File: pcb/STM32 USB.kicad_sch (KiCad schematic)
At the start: 8 parts, among them U1 STM32L432KBUx

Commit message: Pushbutton for reset
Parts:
- added C8: 0.1uF, Capacitor_SMD:C_0201_0603Metric, symbol Device:C
- added SW1: 222AMVBAR, SO4_222A-M-V-B_CTS, symbol 222AMVBAR:222AMVBAR
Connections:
- net GND: now also C8.2, SW1.4
- net NRST: now also C8.1, SW1.3

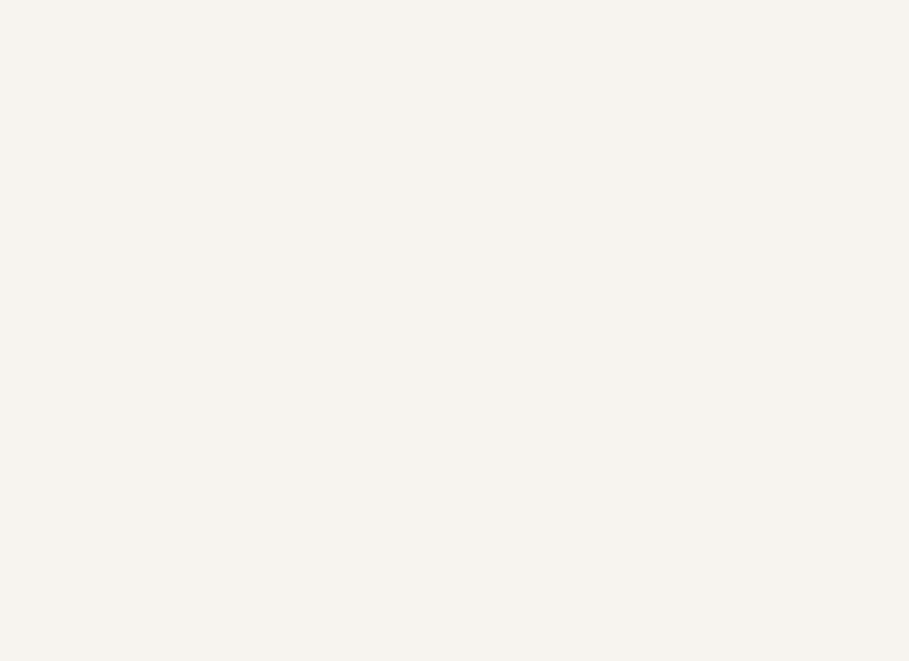
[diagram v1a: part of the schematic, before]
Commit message: Added USB C components to schematic
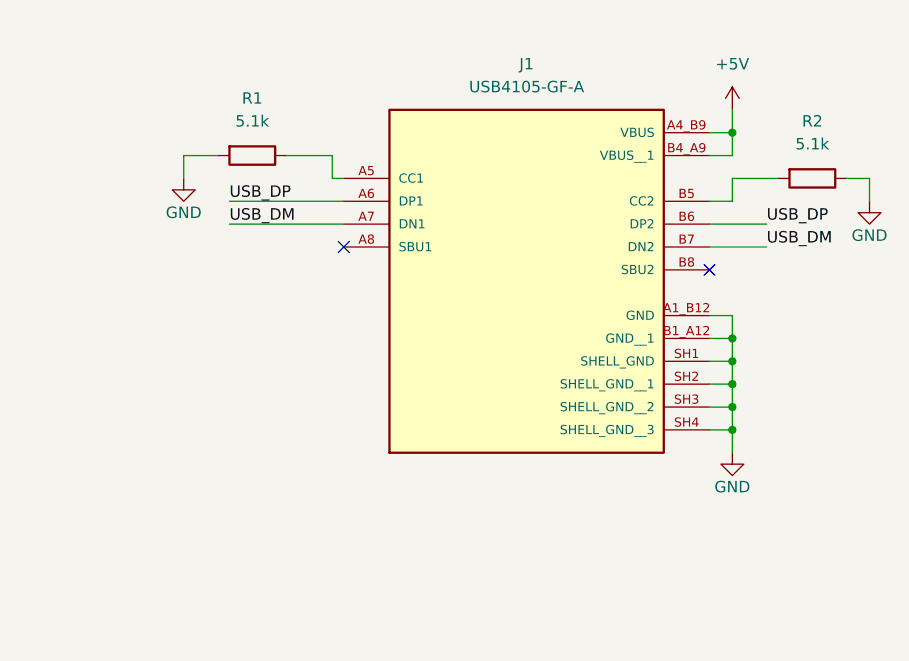
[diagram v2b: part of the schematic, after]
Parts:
- added J1: USB4105-GF-A, USB4105-GF-A:GCT_USB4105-GF-A, symbol USB4105-GF-A:USB4105-GF-A
- added R1, R2: 5.1k, Resistor_SMD:R_0603_1608Metric_Pad0.98x0.95mm_HandSolder, symbol Device:R
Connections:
- net GND: now also J1.A1_B12 (GND), J1.B1_A12 (GND__1), J1.SH1 (SHELL_GND), J1.SH2 (SHELL_GND__1), J1.SH3 (SHELL_GND__2), J1.SH4 (SHELL_GND__3), R1.2, R2.1
- net USB_DM: now also J1.A7 (DN1), J1.B7 (DN2)
- net USB_DP: now also J1.A6 (DP1), J1.B6 (DP2)
- new net: J1.A5 (CC1), R1.1
- new net: J1.B5 (CC2), R2.2
- new net +5V: J1.A4_B9 (VBUS), J1.B4_A9 (VBUS__1)
- no-connect marks 0 -> 2

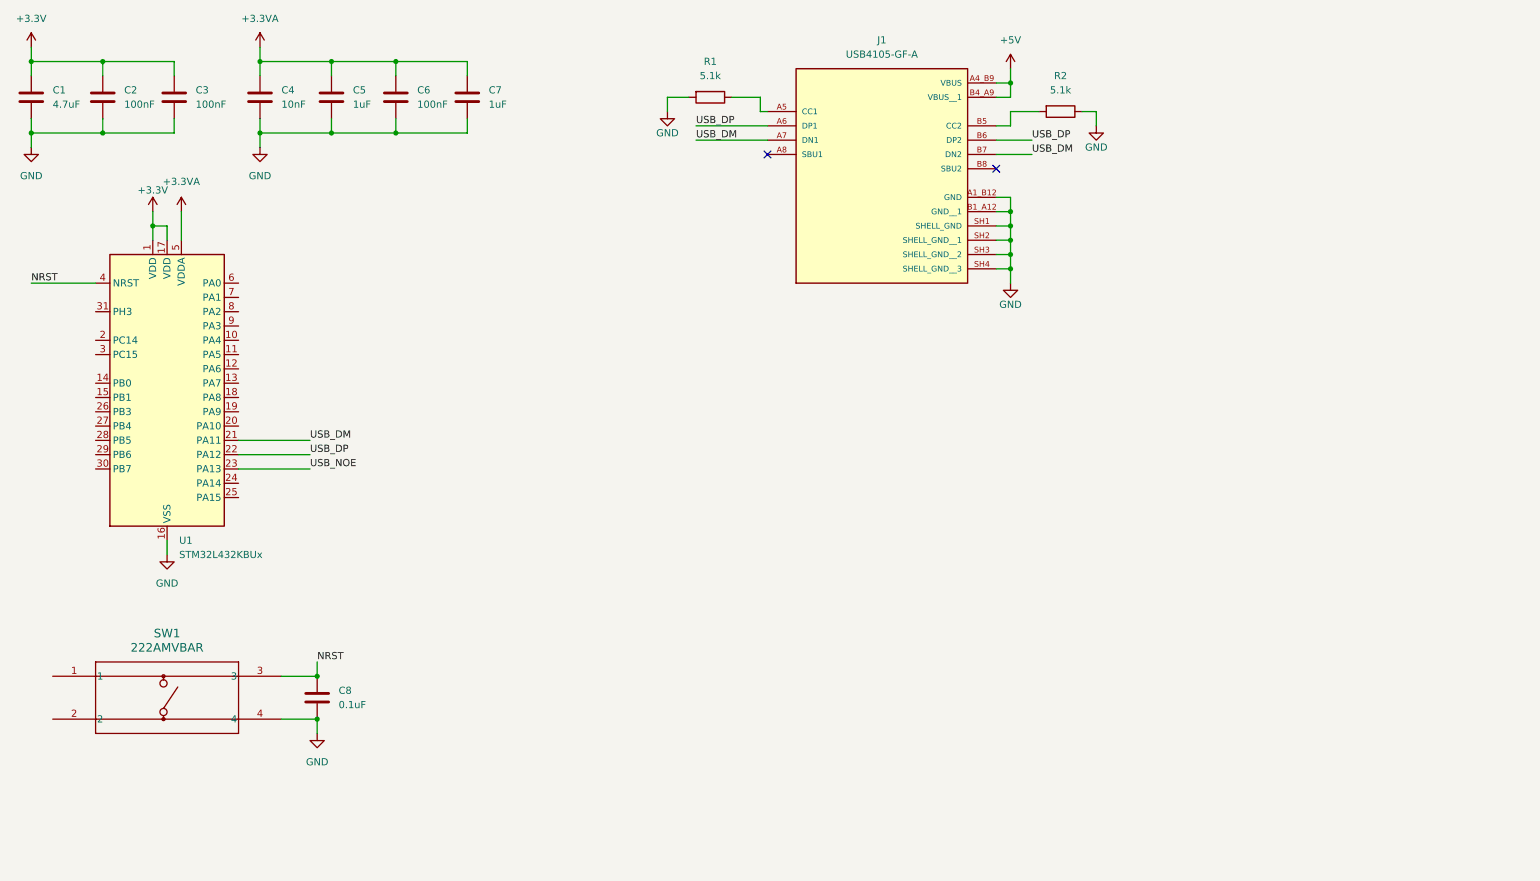
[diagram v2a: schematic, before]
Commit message: Voltage regulator schematic
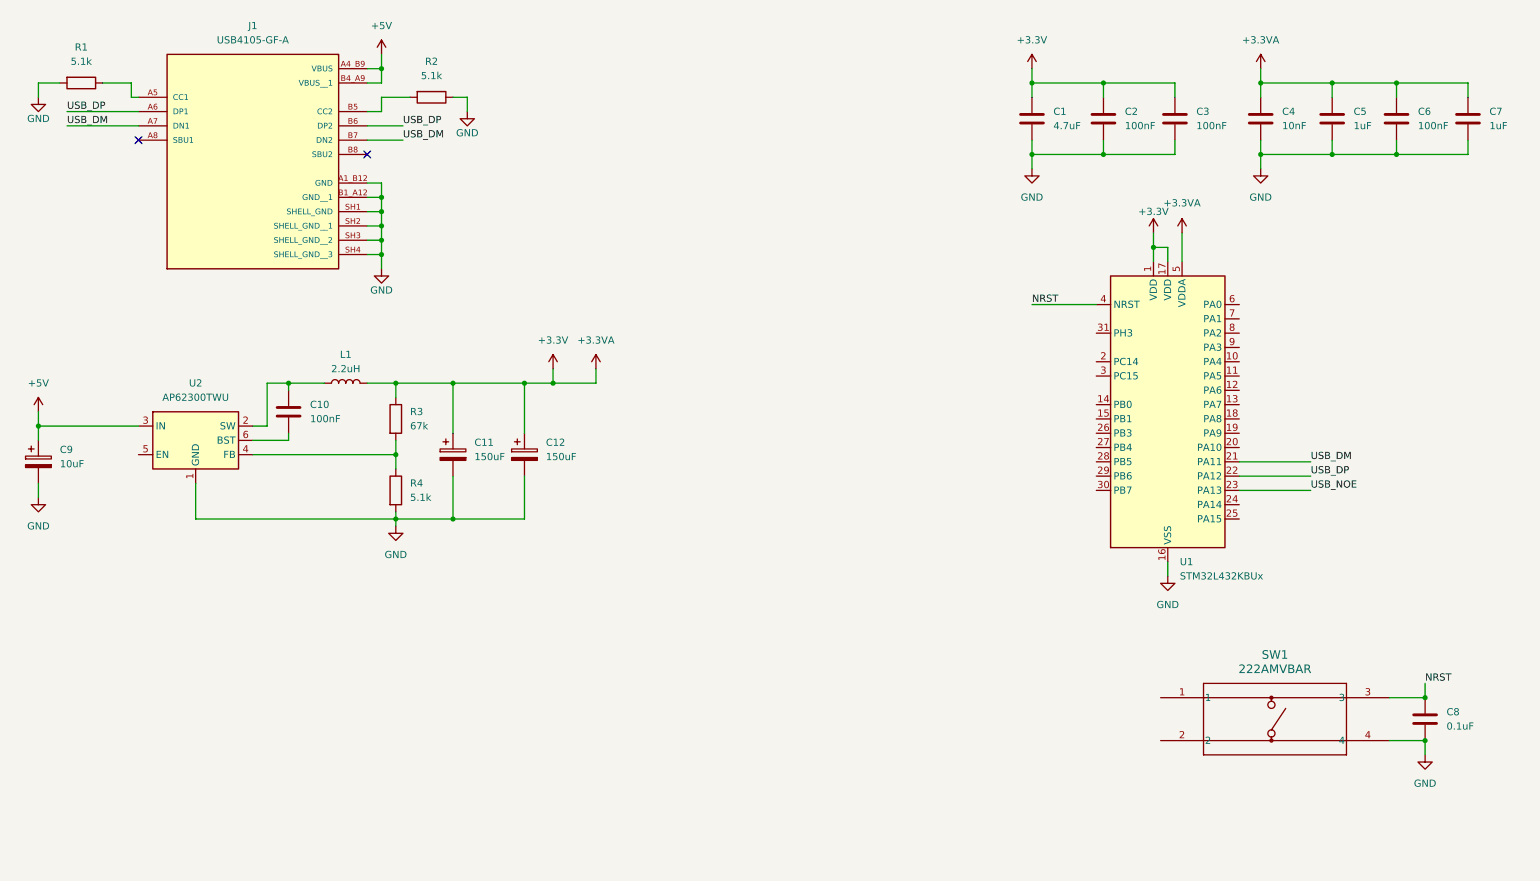
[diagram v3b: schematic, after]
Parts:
- added C10: 100nF, Capacitor_SMD:C_0201_0603Metric, symbol Device:C
- added C11, C12: 150uF, Capacitor_SMD:CP_Elec_10x10, symbol Device:C_Polarized
- added C9: 10uF, Capacitor_SMD:CP_Elec_5x5.3, symbol Device:C_Polarized
- added L1: 2.2uH, Inductor_SMD:L_0603_1608Metric_Pad1.05x0.95mm_HandSolder, symbol Device:L
- added R3: 67k, Resistor_SMD:R_0603_1608Metric_Pad0.98x0.95mm_HandSolder, symbol Device:R
- added R4: 5.1k, Resistor_SMD:R_0603_1608Metric_Pad0.98x0.95mm_HandSolder, symbol Device:R
- added U2: AP62300TWU, Package_TO_SOT_SMD:TSOT-23-6, symbol Regulator_Switching:AP62300TWU
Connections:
- net +3.3VA is gone; now on net +3.3V: C4.1, C5.1, C6.1, C7.1, U1.5 (VDDA)
- net +3.3V: now also C11.1, C12.1, L1.2, R3.1
- net +5V: now also C9.1, U2.3 (IN)
- net GND: now also C11.2, C12.2, C9.2, R4.2, U2.1 (GND)
- new net: R3.2, R4.1, U2.4 (FB)
- new net: C10.1, L1.1, U2.2 (SW)
- new net: C10.2, U2.6 (BST)
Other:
- moved on the sheet: C1, C2, C3, C4, C5, C6, C7, C8, J1, R1, R2, SW1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

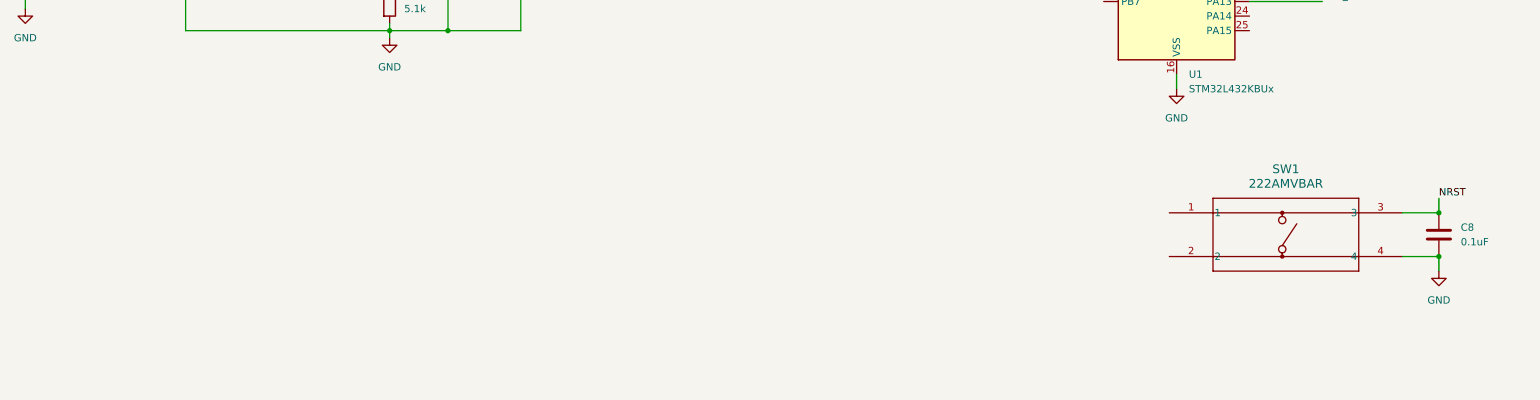
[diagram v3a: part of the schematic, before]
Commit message: Added user pushbutton
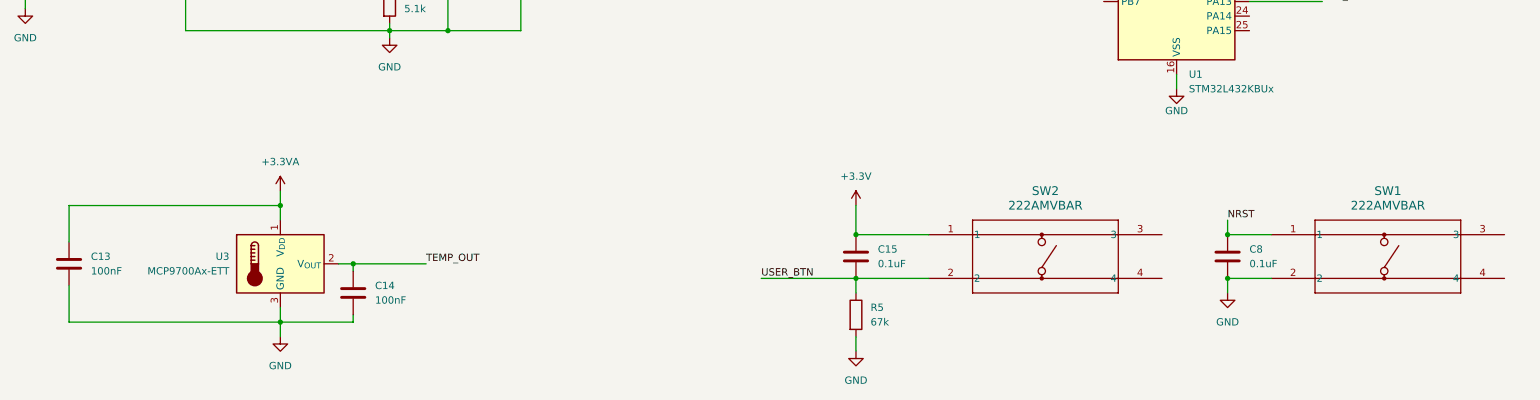
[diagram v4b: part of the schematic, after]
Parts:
- added C13, C14: 100nF, Capacitor_SMD:C_0201_0603Metric, symbol Device:C
- added C15: 0.1uF, Capacitor_SMD:C_0201_0603Metric, symbol Device:C
- added R5: 67k, Resistor_SMD:R_0603_1608Metric_Pad0.98x0.95mm_HandSolder, symbol Device:R
- added SW2: 222AMVBAR, SO4_222A-M-V-B_CTS, symbol 222AMVBAR:222AMVBAR
- added U3: MCP9700Ax-ETT, Package_TO_SOT_SMD:SOT-23, symbol Sensor_Temperature:MCP9700Ax-ETT
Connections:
- net +3.3V: now also C13.1, C15.1, SW2.1, U3.1 (V_{DD})
- net GND: now also SW1.2, C13.2, C14.2, R5.2, U3.3 (GND); no longer SW1.4
- net NRST: now also SW1.1; no longer SW1.3
- new net TEMP_OUT: C14.1, U3.2 (V_{OUT})
- new net USER_BTN: C15.2, R5.1, SW2.2
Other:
- moved on the sheet: C8, SW1

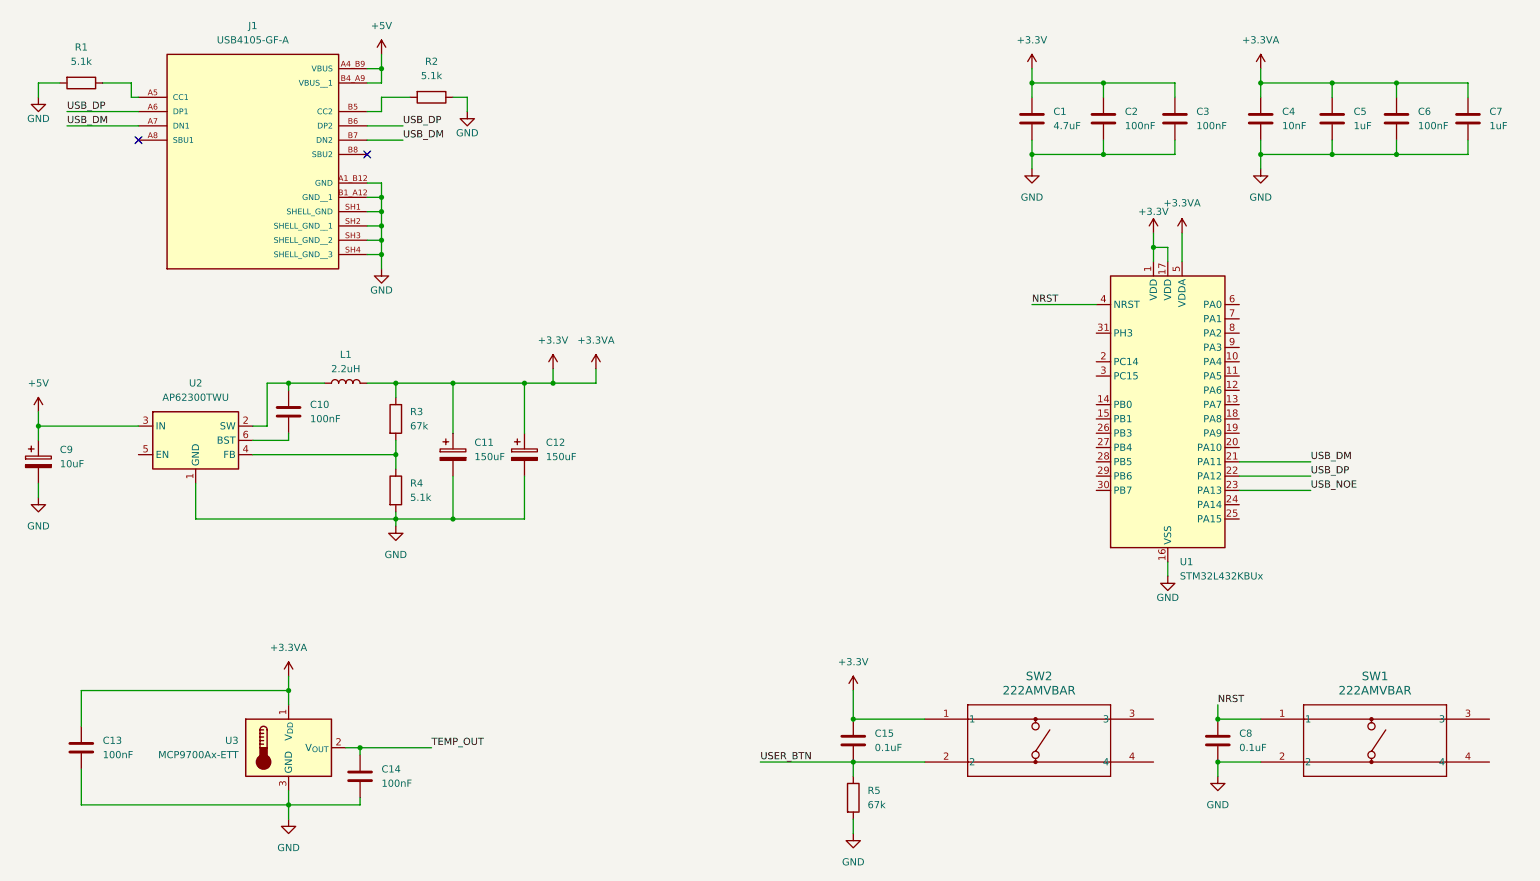
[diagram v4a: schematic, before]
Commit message: Added pin connectors
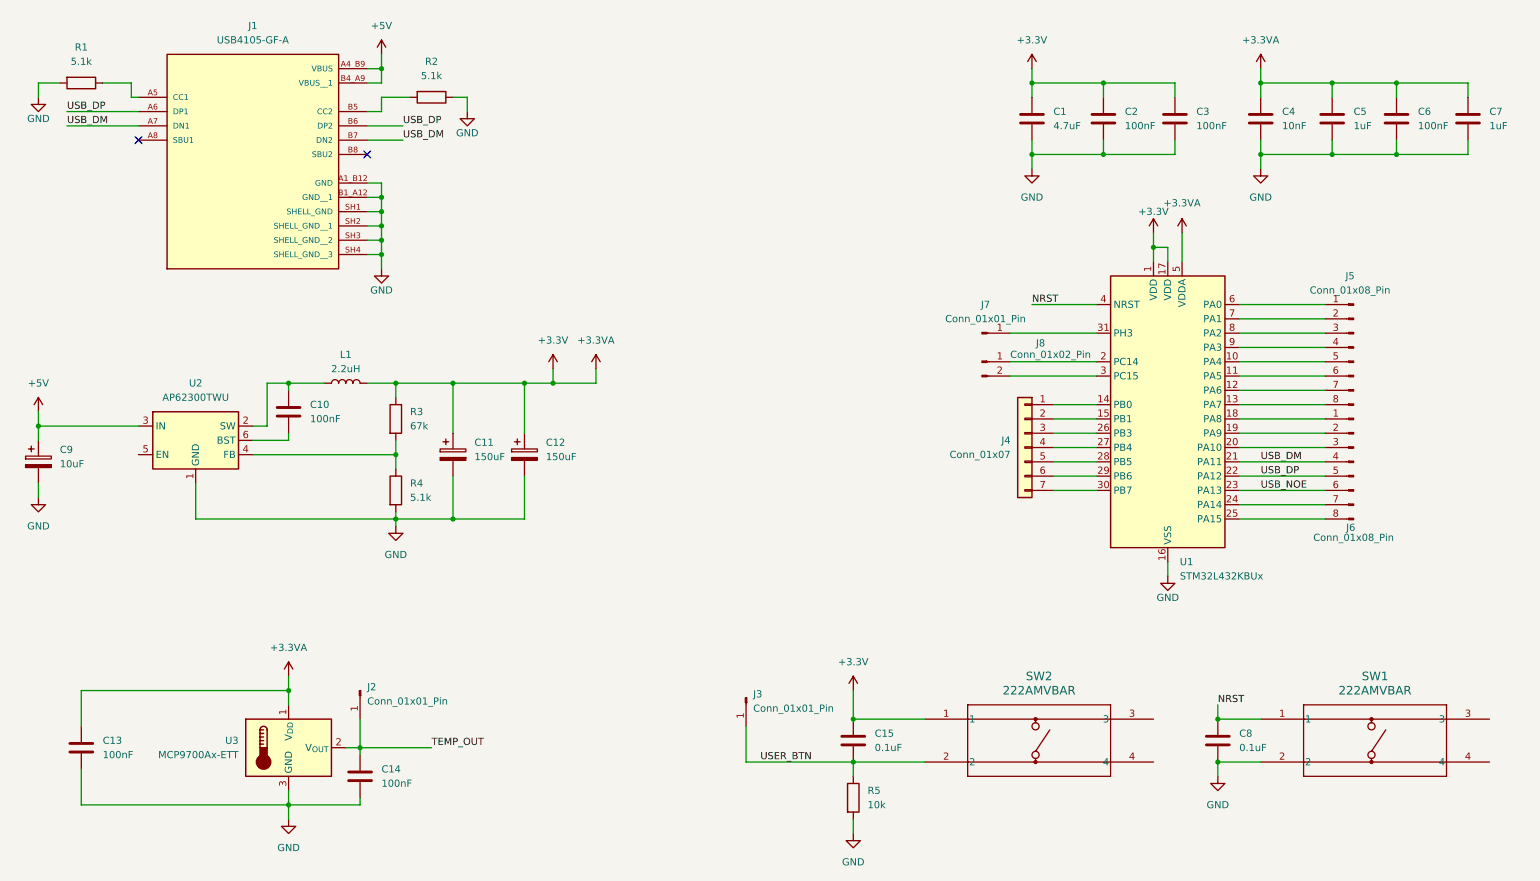
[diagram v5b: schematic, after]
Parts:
- added J2, J3, J7: Conn_01x01_Pin, Connector_PinHeader_2.54mm:PinHeader_1x01_P2.54mm_Vertical, symbol Connector:Conn_01x01_Pin
- added J4: Conn_01x07, Connector_PinSocket_2.54mm:PinSocket_1x07_P2.54mm_Vertical, symbol Connector_Generic:Conn_01x07
- added J5, J6: Conn_01x08_Pin, Connector_PinSocket_2.54mm:PinSocket_1x08_P2.54mm_Vertical, symbol Connector:Conn_01x08_Pin
- added J8: Conn_01x02_Pin, Connector_PinHeader_2.54mm:PinHeader_1x02_P2.54mm_Vertical, symbol Connector:Conn_01x02_Pin
- R5: value 67k -> 10k
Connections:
- net TEMP_OUT: now also J2.1 (Pin_1)
- net USB_DM: now also J6.4 (Pin_4)
- net USB_DP: now also J6.5 (Pin_5)
- net USB_NOE: now also J6.6 (Pin_6)
- net USER_BTN: now also J3.1 (Pin_1)
- net at U1.10 (PA4): now also J5.5 (Pin_5)
- net at U1.11 (PA5): now also J5.6 (Pin_6)
- net at U1.12 (PA6): now also J5.7 (Pin_7)
- net at U1.13 (PA7): now also J5.8 (Pin_8)
- net at U1.14 (PB0): now also J4.1 (Pin_1)
- net at U1.15 (PB1): now also J4.2 (Pin_2)
- net at U1.18 (PA8): now also J6.1 (Pin_1)
- net at U1.19 (PA9): now also J6.2 (Pin_2)
- net at U1.2 (PC14): now also J8.1 (Pin_1)
- net at U1.20 (PA10): now also J6.3 (Pin_3)
- net at U1.24 (PA14): now also J6.7 (Pin_7)
- net at U1.25 (PA15): now also J6.8 (Pin_8)
- net at U1.26 (PB3): now also J4.3 (Pin_3)
- net at U1.27 (PB4): now also J4.4 (Pin_4)
- net at U1.28 (PB5): now also J4.5 (Pin_5)
- net at U1.29 (PB6): now also J4.6 (Pin_6)
- net at U1.3 (PC15): now also J8.2 (Pin_2)
- net at U1.30 (PB7): now also J4.7 (Pin_7)
- net at U1.31 (PH3): now also J7.1 (Pin_1)
- net at U1.6 (PA0): now also J5.1 (Pin_1)
- net at U1.7 (PA1): now also J5.2 (Pin_2)
- net at U1.8 (PA2): now also J5.3 (Pin_3)
- net at U1.9 (PA3): now also J5.4 (Pin_4)

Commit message: Routed PCB
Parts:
- removed J4: Conn_01x07, Connector_PinSocket_2.54mm:PinSocket_1x07_P2.54mm_Vertical, symbol Connector_Generic:Conn_01x07
- added J4: Conn_01x07_Pin, Connector_PinHeader_2.54mm:PinHeader_1x07_P2.54mm_Vertical, symbol Connector:Conn_01x07_Pin
- J1: footprint USB4105-GF-A:GCT_USB4105-GF-A -> footprints:GCT_USB4105-GF-A
- J5, J6: footprint Connector_PinSocket_2.54mm:PinSocket_1x08_P2.54mm_Vertical -> Connector_PinHeader_2.54mm:PinHeader_1x08_P2.54mm_Vertical
- R4: value 5.1k -> 20k
- SW1, SW2: footprint SO4_222A-M-V-B_CTS -> footprints:222AMVBAR
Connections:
- net +3.3V: now also SW2.3
- net GND: now also SW1.4
- net NRST: now also SW1.3
- net USER_BTN: now also SW2.4
- net at U1.14 (PB0): now also J4.1 (Pin_1)
- net at U1.15 (PB1): now also J4.2 (Pin_2)
- net at U1.26 (PB3): now also J4.3 (Pin_3)
- net at U1.27 (PB4): now also J4.4 (Pin_4)
- net at U1.28 (PB5): now also J4.5 (Pin_5)
- net at U1.29 (PB6): now also J4.6 (Pin_6)
- net at U1.30 (PB7): now also J4.7 (Pin_7)
- no-connect marks 2 -> 3
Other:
- moved on the sheet: C15, C8, J3, J7, J8, R5, SW1, SW2
